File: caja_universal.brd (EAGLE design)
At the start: 100 x 99 mm, 45 parts, among them IC1 NE5534, IC2 AD620N, IC3 TL084P, IC4 TL084P, IC5 NE5534, IC6 TL072, J1 +12V-FUSE, J10 POT-OFFSET, J11 POT-GAIN, J12 I-PLACA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

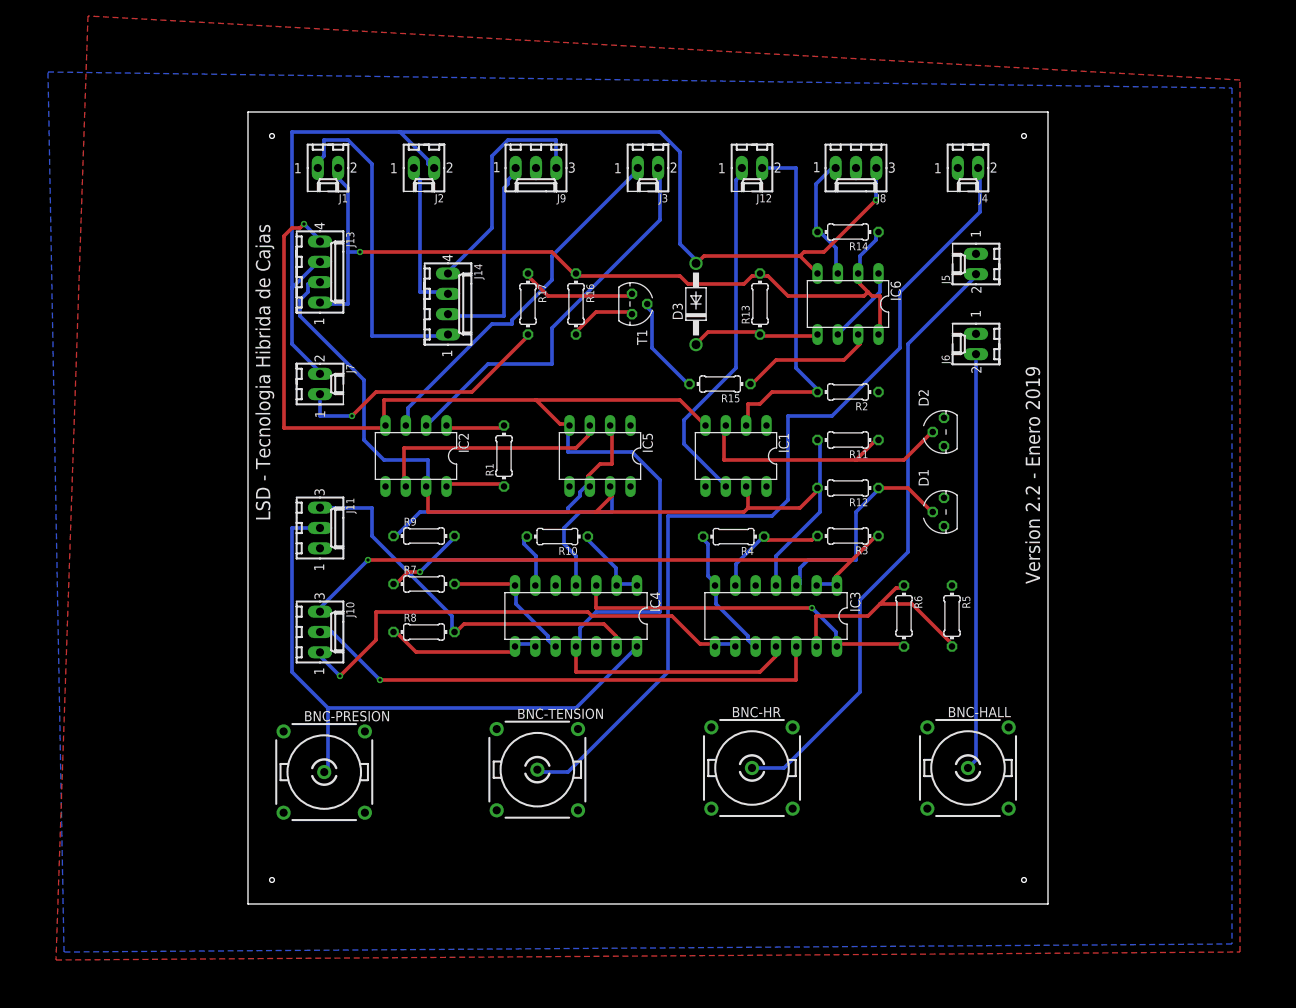
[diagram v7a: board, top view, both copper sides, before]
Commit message: Agrego rectangulo en capa MEASURES para generar la capa profile en el Gerber
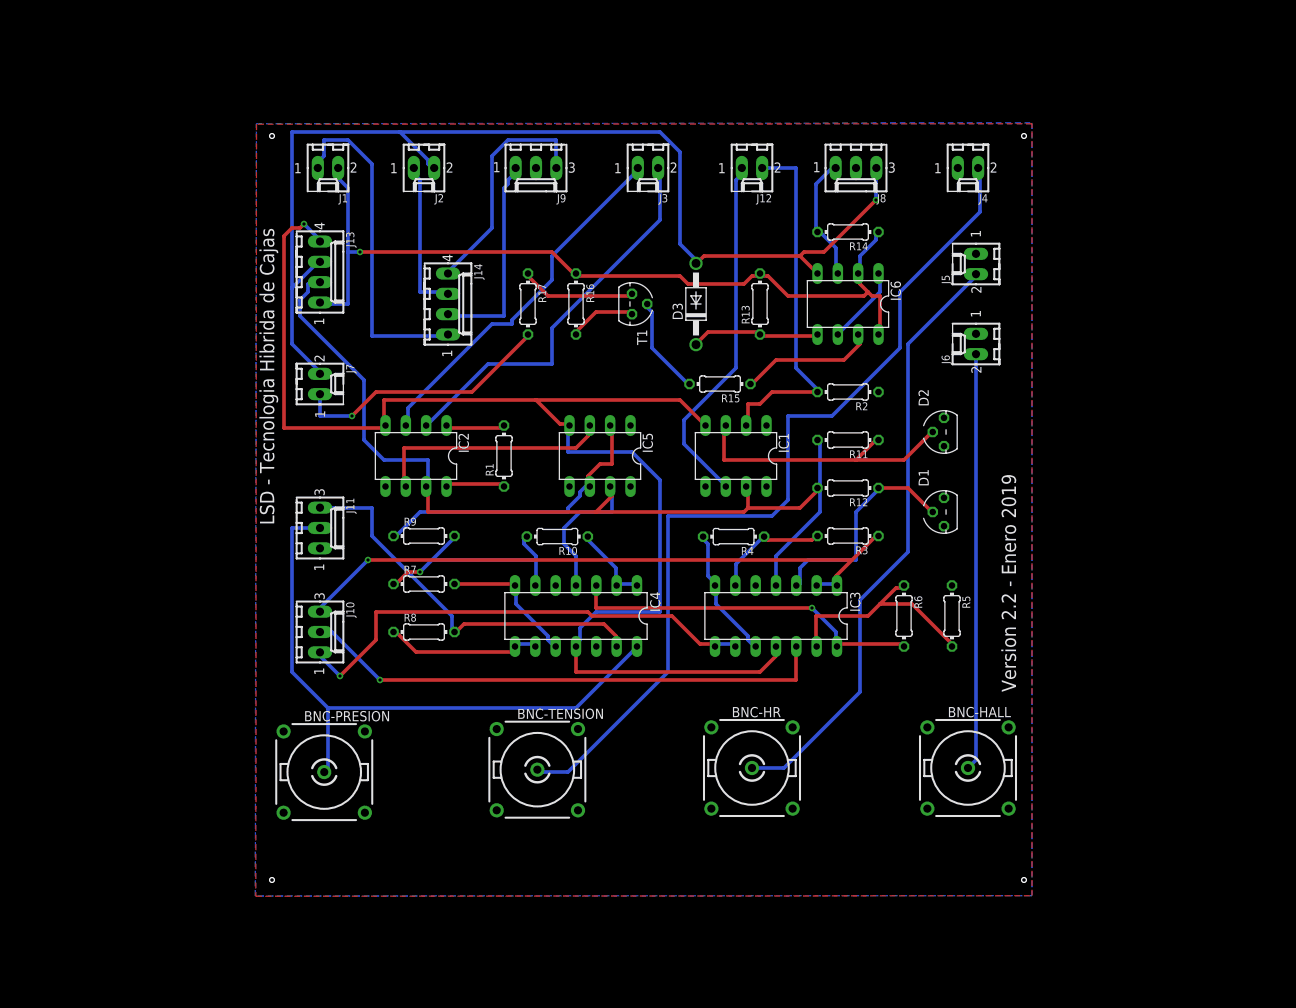
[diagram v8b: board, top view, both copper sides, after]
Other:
- board outline removed
